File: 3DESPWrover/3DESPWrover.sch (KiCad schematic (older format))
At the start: 21 parts, among them J1 Conn_01x05_Male, J2 Conn_01x04, J3 Conn_02x03_Odd_Even, J4 Conn_02x07_Odd_Even, SW1 SW_Push, SW2 SW_Push, U1 ESP32-S2-WROVER

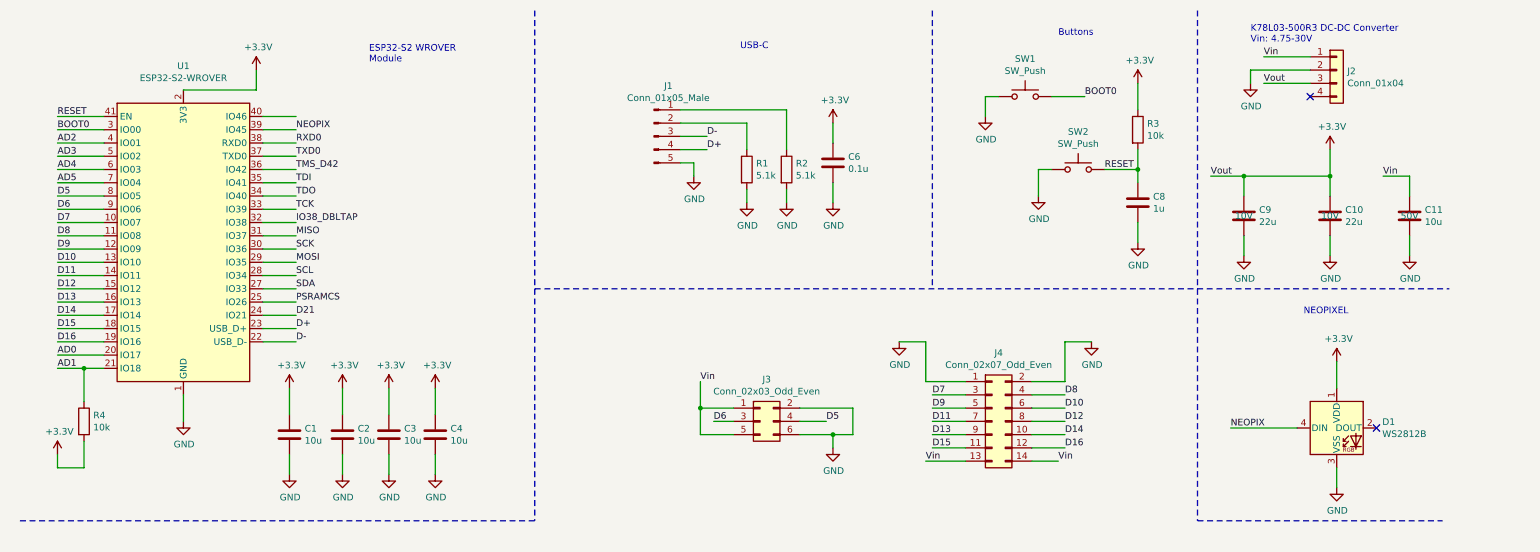
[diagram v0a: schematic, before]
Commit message: Some components replaced by SMD versions
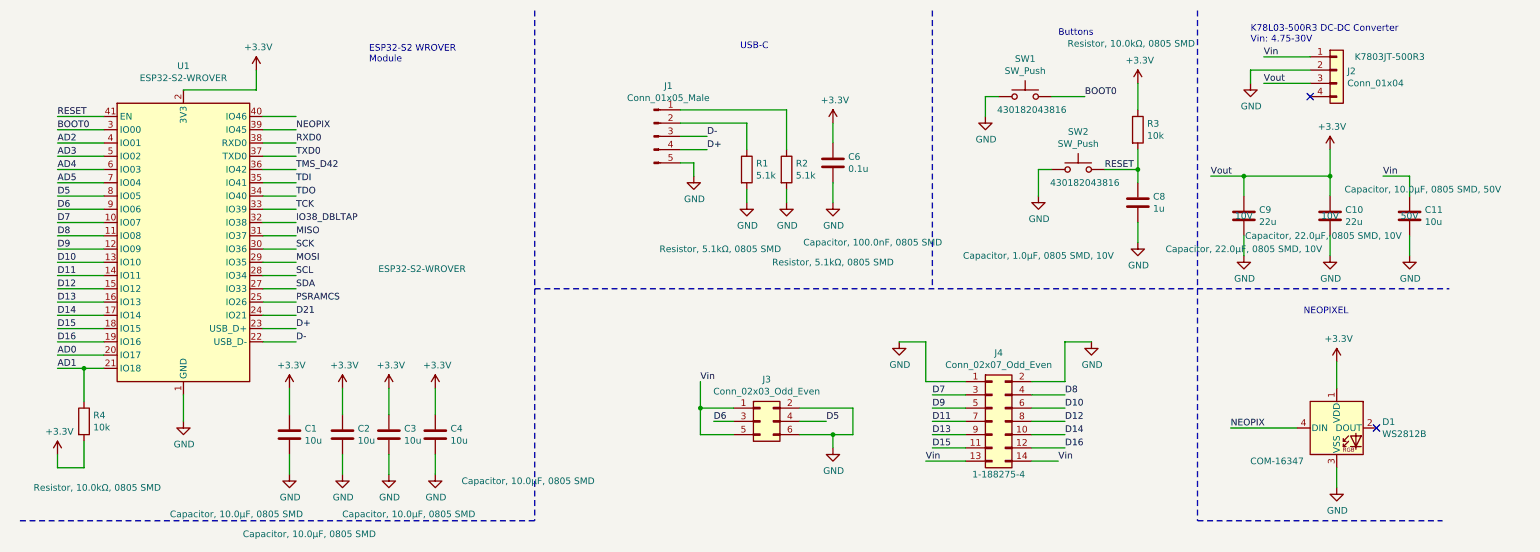
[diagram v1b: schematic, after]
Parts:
- C1, C2, C3, C4: MPN (none) -> Capacitor, 10.0µF, 0805 SMD
- C10, C9: MPN (none) -> Capacitor, 22.0µF, 0805 SMD, 10V
- C11: MPN (none) -> Capacitor, 10.0µF, 0805 SMD, 50V
- C6: MPN (none) -> Capacitor, 100.0nF, 0805 SMD
- C8: MPN (none) -> Capacitor, 1.0µF, 0805 SMD, 10V
- D1: MPN (none) -> COM-16347
- J2: MPN (none) -> K7803JT-500R3
- J4: MPN (none) -> 1-188275-4
- R1, R2: MPN (none) -> Resistor, 5.1kΩ, 0805 SMD
- R3, R4: MPN (none) -> Resistor, 10.0kΩ, 0805 SMD
- SW1, SW2: MPN (none) -> 430182043816
- U1: MPN (none) -> ESP32-S2-WROVER
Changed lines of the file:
@@
 F 2 "RF_Module:ESP32-S2-WROVER" H 2450 1100 50  0001 C CNN
 F 3 "https://www.espressif.com/sites/default/files/documentation/esp32-s2-wrover_esp32-s2-wrover-i_datasheet_en.pdf" H 1400 1450 50  0001 C CNN
+F 4 "ESP32-S2-WROVER" H 3500 2100 50  0000 C CNN "MPN"
 	1    1700 2250
 	1    0    0    -1
@@
 F 2 "Capacitor_SMD:C_0805_2012Metric_Pad1.18x1.45mm_HandSolder" H 2538 3500 50  0001 C CNN
 F 3 "~" H 2500 3650 50  0001 C CNN
+F 4 "Capacitor, 10.0µF, 0805 SMD " H 2100 3050 50  0000 C CNN "MPN"
 	1    2500 3650
 	1    0    0    -1
@@
 F 2 "Capacitor_SMD:C_0805_2012Metric_Pad1.18x1.45mm_HandSolder" H 2938 3500 50  0001 C CNN
 F 3 "~" H 2900 3650 50  0001 C CNN
+F 4 "Capacitor, 10.0µF, 0805 SMD " H 2650 2900 50  0000 C CNN "MPN"
 	1    2900 3650
 	1    0    0    -1
@@
 F 2 "Capacitor_SMD:C_0805_2012Metric_Pad1.18x1.45mm_HandSolder" H 3288 3500 50  0001 C CNN
 F 3 "~" H 3250 3650 50  0001 C CNN
+F 4 "Capacitor, 10.0µF, 0805 SMD " H 3400 3050 50  0000 C CNN "MPN"
 	1    3250 3650
 	1    0    0    -1
@@
 F 2 "Capacitor_SMD:C_0805_2012Metric_Pad1.18x1.45mm_HandSolder" H 3638 3500 50  0001 C CNN
 F 3 "~" H 3600 3650 50  0001 C CNN
+F 4 "Capacitor, 10.0µF, 0805 SMD " H 4300 3300 50  0000 C CNN "MPN"
 	1    3600 3650
 	1    0    0    -1
@@
 F 3 "~" H 9700 2000 50  0001 C CNN
 F 4 "10V" H 9700 2000 50  0000 C CNN "Voltage"
+F 5 "Capacitor, 22.0µF, 0805 SMD, 10V " H 9700 1750 50  0000 C CNN "MPN"
 	1    9700 2000
 	1    0    0    -1
@@
 F 3 "~" H 10350 2000 50  0001 C CNN
 F 4 "10V" H 10350 2000 50  0000 C CNN "Voltage"
+F 5 "Capacitor, 22.0µF, 0805 SMD, 10V " H 10300 1850 50  0000 C CNN "MPN"
 	1    10350 2000
 	1    0    0    -1
@@
 F 3 "~" H 10950 2000 50  0001 C CNN
 F 4 "50V" H 10950 2000 50  0000 C CNN "Voltage"
+F 5 "Capacitor, 10.0µF, 0805 SMD, 50V " H 11050 2200 50  0000 C CNN "MPN"
 	1    10950 2000
 	1    0    0    -1
@@
 F 2 "Button_Switch_SMD:SW_SPST_B3S-1000" H 8450 1850 50  0001 C CNN
 F 3 "~" H 8450 1850 50  0001 C CNN
+F 4 "430182043816" H 8500 1550 50  0000 C CNN "MPN"
 	1    8450 1650
 	1    0    0    -1
@@
 F 2 "Button_Switch_SMD:SW_SPST_B3S-1000" H 8050 1300 50  0001 C CNN
 F 3 "~" H 8050 1300 50  0001 C CNN
+F 4 "430182043816" H 8100 1000 50  0000 C CNN "MPN"
 	1    8050 1100
 	1    0    0    -1
@@
 F 2 "Capacitor_SMD:C_0805_2012Metric_Pad1.18x1.45mm_HandSolder" H 8938 1750 50  0001 C CNN
 F 3 "~" H 8900 1900 50  0001 C CNN
+F 4 "Capacitor, 1.0µF, 0805 SMD, 10V " H 8150 1500 50  0000 C CNN "MPN"
 	1    8900 1900
 	1    0    0    -1
@@
 F 2 "Resistor_SMD:R_0805_2012Metric_Pad1.20x1.40mm_HandSolder" V 8830 1350 50  0001 C CNN
 F 3 "~" H 8900 1350 50  0001 C CNN
+F 4 "Resistor, 10.0kΩ, 0805 SMD " H 8850 2000 50  0000 C CNN "MPN"
 	1    8900 1350
 	1    0    0    -1
@@
 F 2 "LED_SMD:LED_WS2812B_PLCC4_5.0x5.0mm_P3.2mm" H 10450 3300 50  0001 L TNN
 F 3 "https://cdn-shop.adafruit.com/datasheets/WS2812B.pdf" H 10500 3225 50  0001 L TNN
+F 4 "COM-16347" H 9950 3350 50  0000 C CNN "MPN"
 	1    10400 3600
 	1    0    0    -1
@@
 F 2 "Resistor_SMD:R_0805_2012Metric_Pad1.20x1.40mm_HandSolder" V 5880 1650 50  0001 C CNN
 F 3 "~" H 5950 1650 50  0001 C CNN
+F 4 "Resistor, 5.1kΩ, 0805 SMD " H 5750 1050 50  0000 C CNN "MPN"
 	1    5950 1650
 	1    0    0    -1
@@
 F 2 "Resistor_SMD:R_0805_2012Metric_Pad1.20x1.40mm_HandSolder" V 6180 1650 50  0001 C CNN
 F 3 "~" H 6250 1650 50  0001 C CNN
+F 4 "Resistor, 5.1kΩ, 0805 SMD " H 6600 950 50  0000 C CNN "MPN"
 	1    6250 1650
 	1    0    0    -1
@@
 F 2 "Capacitor_SMD:C_0805_2012Metric_Pad1.18x1.45mm_HandSolder" H 6638 1450 50  0001 C CNN
 F 3 "~" H 6600 1600 50  0001 C CNN
+F 4 "Capacitor, 100.0nF, 0805 SMD" H 6900 1000 50  0000 C CNN "MPN"
 	1    6600 1600
 	1    0    0    -1
@@
 F 2 "Custom:TE_Micromatch_2,54_14_SMD" H 7800 3550 50  0001 C CNN
 F 3 "~" H 7800 3550 50  0001 C CNN
+F 4 "1-188275-4" H 7850 3150 50  0000 C CNN "MPN"
 	1    7800 3550
 	1    0    0    -1
@@
 F 2 "Resistor_SMD:R_0805_2012Metric_Pad1.20x1.40mm_HandSolder" V 880 3550 50  0001 C CNN
 F 3 "~" H 950 3550 50  0001 C CNN
+F 4 " Resistor, 10.0kΩ, 0805 SMD " H 1050 3050 50  0000 C CNN "MPN"
 	1    950  3550
 	1    0    0    -1
@@
 F 2 "Custom:K7803JT-500R3-SMD" H 10400 900 50  0001 C CNN
 F 3 "~" H 10400 900 50  0001 C CNN
+F 4 "K7803JT-500R3" H 10800 1000 50  0000 C CNN "MPN"
 	1    10400 900
 	1    0    0    -1
